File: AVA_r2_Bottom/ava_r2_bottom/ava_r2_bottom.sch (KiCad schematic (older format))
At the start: 21 parts, among them J1 RC_Radio, J2 UART_RxTx_5V, J3 I2C_SdaScl_3V, J4 5V_IN, J5 GND_IN, U1 MPU6500, U2 Teensy4.1, U3 MPL3115A2

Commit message: update laptop
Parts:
- U2: symbol teensy:Teensy4.1 -> ava_r2_bottom-rescue:Teensy4.1-teensy
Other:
- note removed: "AVA Revision 2 Bottom PCB\n"
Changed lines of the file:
@@
 encoding utf-8
 Sheet 1 1
-Title ""
-Date ""
-Rev ""
+Title "AVA Flight Controller "
+Date "2021-05-10"
+Rev "2"
 Comp ""
 Comment1 ""
@@
 $EndComp
 $Comp
-L teensy:Teensy4.1 U2
+L ava_r2_bottom-rescue:Teensy4.1-teensy U2
 U 1 1 60990CDB
 P 9250 4100
@@
 Wire Wire Line
 	6100 4350 6200 4350
-Text Notes 7350 7500 0    71   ~ 0
-AVA Revision 2 Bottom PCB\n
 $Comp
 L Connector:Conn_01x01_Male J4

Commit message: update
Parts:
- added J6: SER1_SER2, Connector_PinHeader_1.27mm:PinHeader_1x06_P1.27mm_Vertical, symbol Connector_Generic:Conn_01x06
- added J7: SER3_SER4, Connector_PinHeader_1.27mm:PinHeader_1x06_P1.27mm_Vertical, symbol Connector_Generic:Conn_01x06
- added J8: SER5_SER6, Connector_PinHeader_1.27mm:PinHeader_1x06_P1.27mm_Vertical, symbol Connector_Generic:Conn_01x06
- C1, C2, C3, C4, C5, C6: footprint (none) -> Capacitor_SMD:C_0805_2012Metric_Pad1.18x1.45mm_HandSolder
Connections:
- net +5V: now also J6.2 (Pin_2), J6.5 (Pin_5), J7.2 (Pin_2), J7.5 (Pin_5), J8.2 (Pin_2), J8.5 (Pin_5)
- net GND: now also J6.3 (Pin_3), J6.6 (Pin_6), J7.3 (Pin_3), J7.6 (Pin_6), J8.3 (Pin_3), J8.6 (Pin_6)
- net SERVO1_PWM: now also J6.1 (Pin_1)
- net SERVO2_PWM: now also J6.4 (Pin_4)
- net SERVO3_PWM: now also J7.1 (Pin_1)
- net SERVO4_PWM: now also J7.4 (Pin_4)
- net SERVO5_PWM: now also J8.1 (Pin_1)
- net SERVO6_PWM: now also J8.4 (Pin_4)
- net P8_TX2_IN1: now reaches U2.10 (8_TX2_IN1)
- net P26_A12_MOSI1: now reaches U2.18 (26_A12_MOSI1)
- net P27_A13_SCK1: now reaches U2.19 (27_A13_SCK1)
- net P0_RX1_CRX2_CS1: now reaches U2.2 (0_RX1_CRX2_CS1)
- net P30_CRX3: now reaches U2.22 (30_CRX3)
- net P31_CTX3: now reaches U2.23 (31_CTX3)
- net P32_OUT1B: now reaches U2.24 (32_OUT1B)
- net P33_MCLK2: now reaches U2.25 (33_MCLK2)
- net P37_CS: now reaches U2.29 (37_CS)
- net P1_TX1_CTX2_MISO1: now reaches U2.3 (1_TX1_CTX2_MISO1)
- net P38_CS1: now reaches U2.30 (38_CS1_IN1)
- net P39_MISO1: now reaches U2.31 (39_MISO1_OUT1A)
- net P41_A16: now reaches U2.32 (40_A16)
- net P41_A17: now reaches U2.33 (41_A17)
- net P14_A0_TX3: now reaches U2.36 (14_A0_TX3_SPDIF_OUT)
- net P15_A1_RX3: now reaches U2.37 (15_A1_RX3_SPDIF_IN)
- net P20_A6_TX5: now reaches U2.42 (20_A6_TX5_LRCLK1)
- net P21_A7_RX5: now reaches U2.43 (21_A7_RX5_BCLK1)
- net VBAT: now reaches U2.50 (VBAT)
- net PROGRAM: now reaches U2.53 (PROGRAM)
- net ON_OFF: now reaches U2.54 (ON_OFF)
- net USBH_5V: now reaches U2.55 (5V)
- net USBH_D-: now reaches U2.56 (D-)
- net USBH_D+: now reaches U2.57 (D+)
- net USBH_GND: now reaches U2.58 (GND)
- net USBH_GND: now also U2.59 (GND)
- net ETH_R+: now reaches U2.60 (R+)
- net ETH_LED: now reaches U2.61 (LED)
- net ETH_T-: now reaches U2.62 (T-)
- net ETH_T+: now reaches U2.63 (T+)
- net ETH_GND: now reaches U2.64 (GND)
- net ETH_R-: now reaches U2.65 (R-)
- net USB_D-: now reaches U2.66 (D-)
- net USB_D+: now reaches U2.67 (D+)
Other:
- moved on the sheet: BZ1, D1, D2, D3, J4, J5, R1, R2, R3

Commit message: PCB Bottom Complete
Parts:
- added P0, P1, P14, P15, P20, P21, P26, P27, P38, P39, P8: TestPoint, TestPoint:TestPoint_Pad_2.0x2.0mm, symbol Connector:TestPoint
- renumbered J3 to I2C1, J1 to RADIO1, J2 to UART1
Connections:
- net P0_RX1_CRX2_CS1: now also P0.1
- net P14_A0_TX3: now also P14.1
- net P15_A1_RX3: now also P15.1
- net P1_TX1_CTX2_MISO1: now also P1.1
- net P20_A6_TX5: now also P20.1
- net P21_A7_RX5: now also P21.1
- net P26_A12_MOSI1: now also P26.1
- net P27_A13_SCK1: now also P27.1
- net P38_CS1: now also P38.1
- net P39_MISO1: now also P39.1
- net P8_TX2_IN1: now also P8.1
- no-connect marks 0 -> 14
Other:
- note added: "Testpads\n"
- moved on the sheet: U2

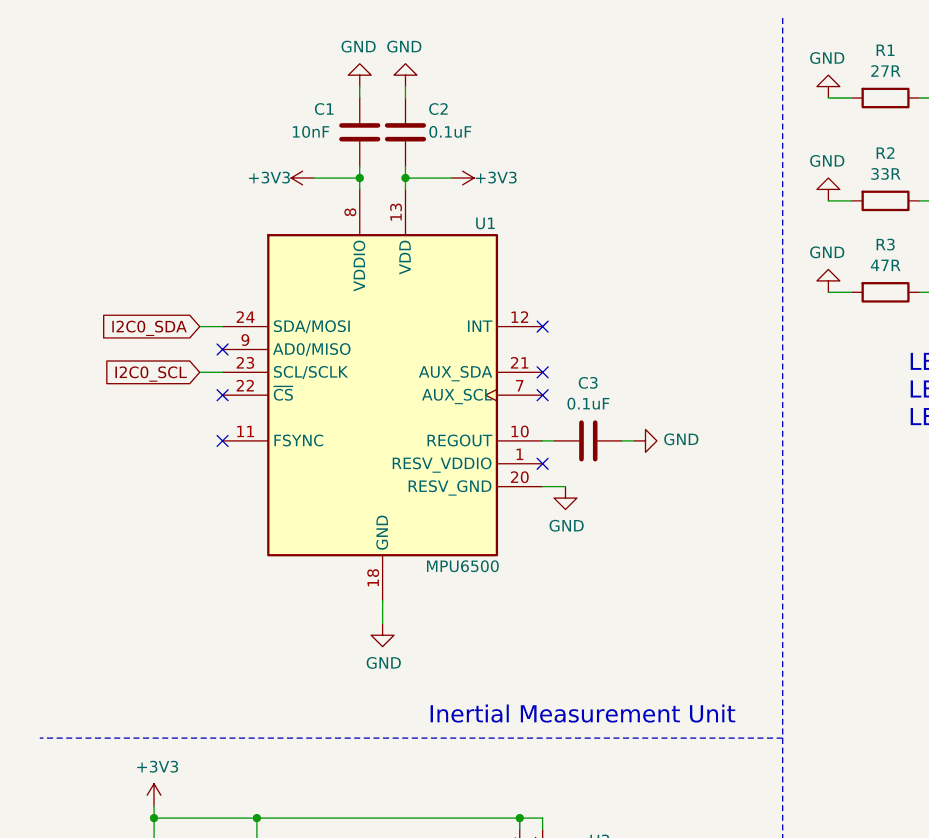
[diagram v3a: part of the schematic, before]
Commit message: added mpu6050
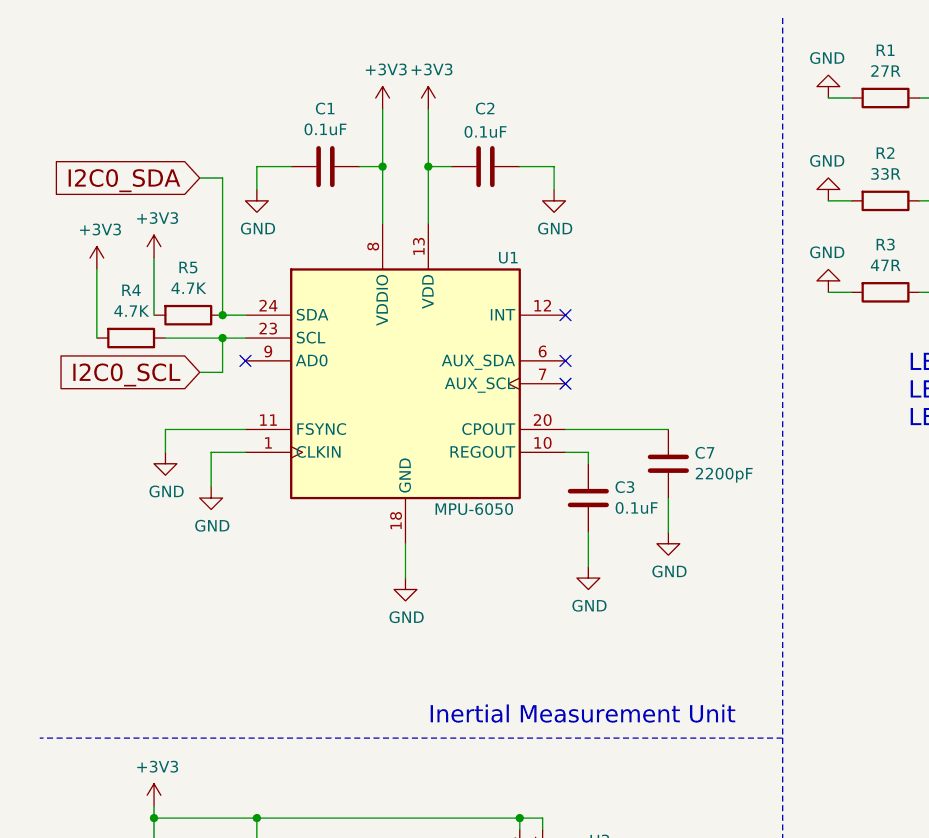
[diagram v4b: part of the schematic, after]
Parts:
- removed U1: MPU6500, Sensor_Motion:InvenSense_QFN-24_3x3mm_P0.4mm, symbol Sensor_Motion:MPU-9250
- added C7: 2200pF, Capacitor_SMD:C_0805_2012Metric_Pad1.18x1.45mm_HandSolder, symbol Device:C
- added R4, R5: 4.7K, Resistor_THT:R_Axial_DIN0207_L6.3mm_D2.5mm_P7.62mm_Horizontal, symbol Device:R
- added U1: MPU-6050, Sensor_Motion:InvenSense_QFN-24_4x4mm_P0.5mm, symbol Sensor_Motion:MPU-6050
- C1: value 10nF -> 0.1uF
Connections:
- net +3V3: now also C1.1, R4.2, R5.2, U1.13 (VDD), U1.8 (VDDIO); no longer C1.2
- net GND: now also C1.2, C3.2, C7.1, U1.1 (CLKIN), U1.11 (FSYNC), U1.18 (GND); no longer C1.1, C3.1
- net I2C0_SCL: now also R4.1, U1.23 (SCL)
- net I2C0_SDA: now also R5.1, U1.24 (SDA)
- new net: C3.1, U1.10 (REGOUT)
- new net: C7.2, U1.20 (CPOUT)
- no-connect marks 14 -> 11
